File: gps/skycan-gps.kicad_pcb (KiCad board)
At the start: 2 copper layers, 50 x 50 mm, 9 parts, among them J1 SMA, U1 Taoglas CGGP.25.A

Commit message: GPS layout finished.
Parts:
- added GAP: VAL**, GAP, F.Cu at (0.00, 0.00)
- added STUB: VAL**, STUB, F.Cu at (0.00, 0.00)
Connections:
- net N-000003 renamed /SGNL
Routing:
- net GND: track 0.00 -> 240.7 mm, vias 0 -> 140
- net /SGNL: track 0.00 -> 19.0 mm

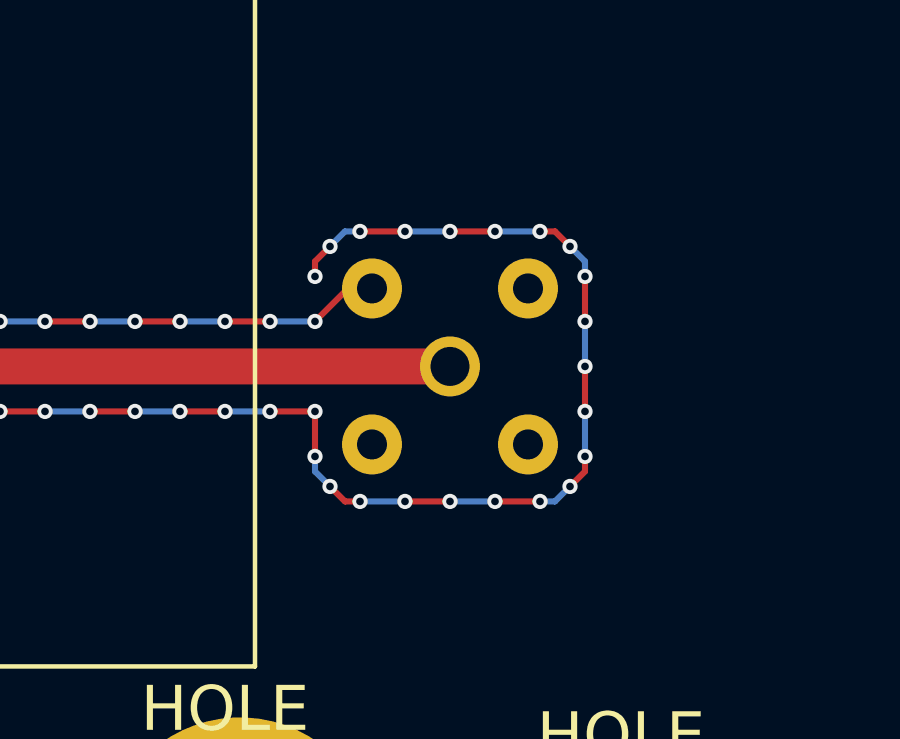
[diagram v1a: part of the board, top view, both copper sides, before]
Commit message: Reworked GPS pcb.
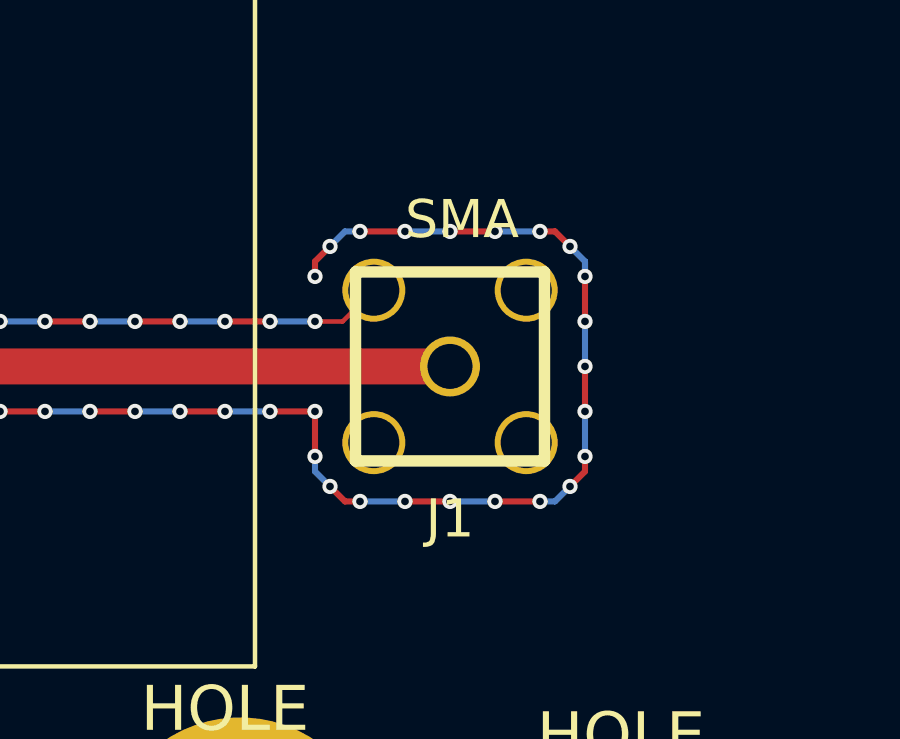
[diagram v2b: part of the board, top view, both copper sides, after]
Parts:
- J1: moved to F.Cu
- moved G*** 18.7 mm to (112.9, 116.5)

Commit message: add two more inner layers to gps
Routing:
- added copper zone on Inner1.Cu, net GND
- added copper zone on Inner2.Cu, net GND
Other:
- copper layers 2 -> 4
- board text added: "4-layer v1.0"
- board text removed: "v1.0"
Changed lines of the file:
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@@
     (links 8)
     (no_connects 0)
-    (area 99.987299 89.987299 150.012701 140.012701)
+    (area -2.3048 -2.2286 150.012701 140.9469)
     (thickness 1.6)
     (drawings 10)
@@
   (layers
     (15 F.Cu signal)
+    (2 Inner2.Cu signal hide)
+    (1 Inner1.Cu signal hide)
     (0 B.Cu signal hide)
     (16 B.Adhes user)
@@
     (user_trace_width 0.2032)
     (user_trace_width 0.254)
-    (user_trace_width 0.3048)
+    (user_trace_width 0.309)
+    (user_trace_width 0.358)
     (user_trace_width 0.4064)
     (user_trace_width 0.8128)
-    (user_trace_width 1.2)
     (trace_clearance 0.1524)
-    (zone_clearance 0.233)
+    (zone_clearance 0.2)
     (zone_45_only no)
     (trace_min 0.1524)
@@
     (visible_elements FFFEFF7F)
     (pcbplotparams
-      (layerselection 284196865)
+      (layerselection 284196871)
       (usegerberextensions true)
       (excludeedgelayer false)
@@
     (effects (font (size 1.27 1.27) (thickness 0.127)) (justify mirror))
   )
-  (gr_text v1.0 (at 127.381 99.06) (layer F.SilkS)
+  (gr_text "4-layer v1.0" (at 125.6 99.2) (layer F.SilkS)
     (effects (font (size 0.635 0.635) (thickness 0.127)))
   )
@@
   (gr_line (start 100 100) (end 110 90) (angle 90) (layer Edge.Cuts) (width 0.0254))
   (gr_line (start 100 130) (end 100 100) (angle 90) (layer Edge.Cuts) (width 0.0254))
-  (segment (start 113 117.5) (end 132 117.5) (width 1.2) (layer F.Cu) (net 1))
+  (segment (start 113 117.5) (end 132 117.5) (width 0.309) (layer F.Cu) (net 1))
   (segment (start 127.5 116) (end 128.42 116) (width 0.1524) (layer F.Cu) (net 2))
   (via (at 136.5 119) (size 0.508) (layers F.Cu B.Cu) (net 2))
@@
     )
   )
-  (zone (net 2) (net_name GND) (layer F.Cu) (hatch edge 0.508)
-    (connect_pads (clearance 0.233))
+  (zone (net 2) (net_name GND) (layer Inner2.Cu) (hatch edge 0.508)
+    (connect_pads (clearance 0.127))
     (min_thickness 0.127)
     (fill (arc_segments 16) (thermal_gap 0.127) (thermal_bridge_width 0.254))
+    (polygon
+      (pts
+        (xy 150 130) (xy 140 140) (xy 110 140) (xy 100 130) (xy 100 100)
+        (xy 110 90) (xy 140 90) (xy 150 100)
+      )
+    )
+  )
+  (zone (net 2) (net_name GND) (layer Inner1.Cu) (hatch edge 0.508)
+    (connect_pads (clearance 0.127))
+    (min_thickness 0.127)
+    (fill (arc_segments 16) (thermal_gap 0.127) (thermal_bridge_width 0.254))
+    (polygon
+      (pts
+        (xy 150 130) (xy 140 140) (xy 110 140) (xy 100 130) (xy 100 100)
+        (xy 110 90) (xy 140 90) (xy 150 100)
+      )
+    )
+  )
+  (zone (net 2) (net_name GND) (layer F.Cu) (hatch edge 0.508)
+    (connect_pads (clearance 0.2))
+    (min_thickness 0.127)
+    (fill (arc_segments 16) (thermal_gap 0.127) (thermal_bridge_width 0.254))
